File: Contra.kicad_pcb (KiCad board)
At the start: 2 copper layers, 251.5 x 76.2 mm, 152 parts, among them J1 Conn_01x03, J2 Conn_01x02, SW1 SW_PUSH, SW2 SW_SPDT, U1 ProMicro

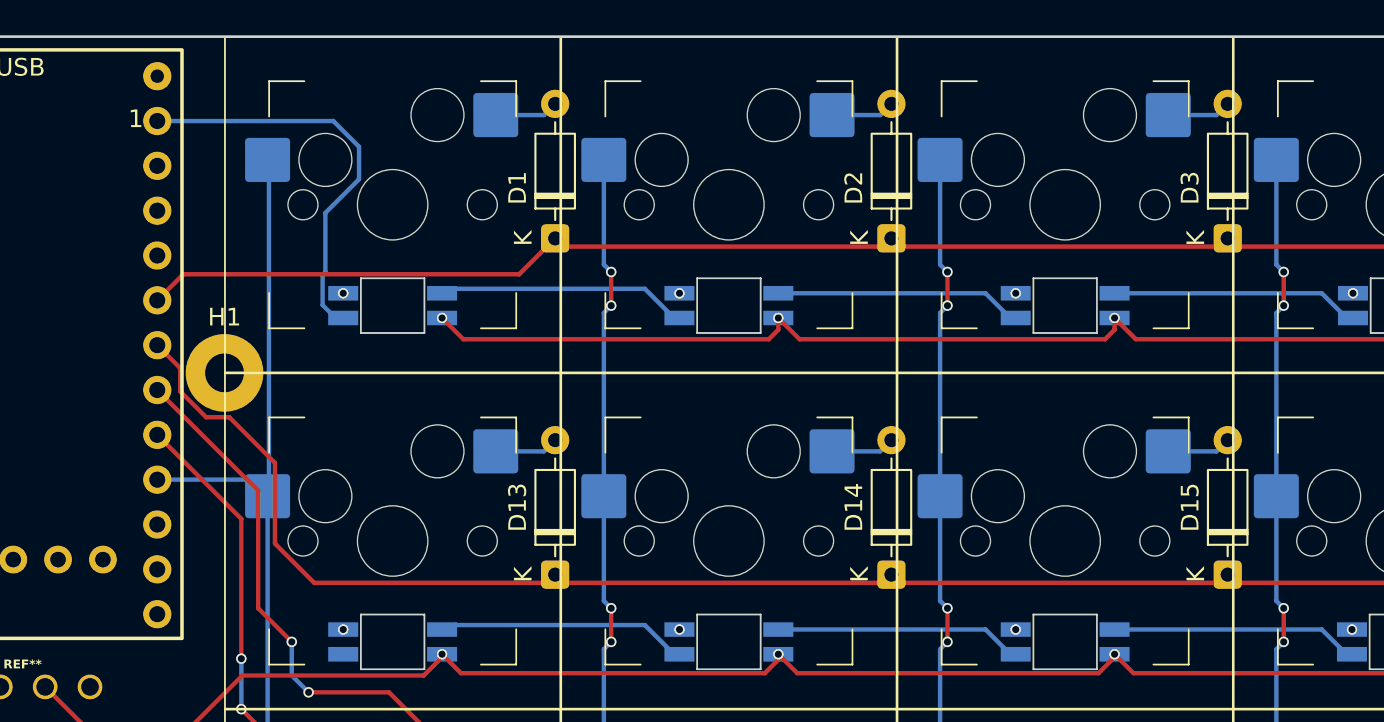
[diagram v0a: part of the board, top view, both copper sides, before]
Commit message: connect col1-3 to mcu
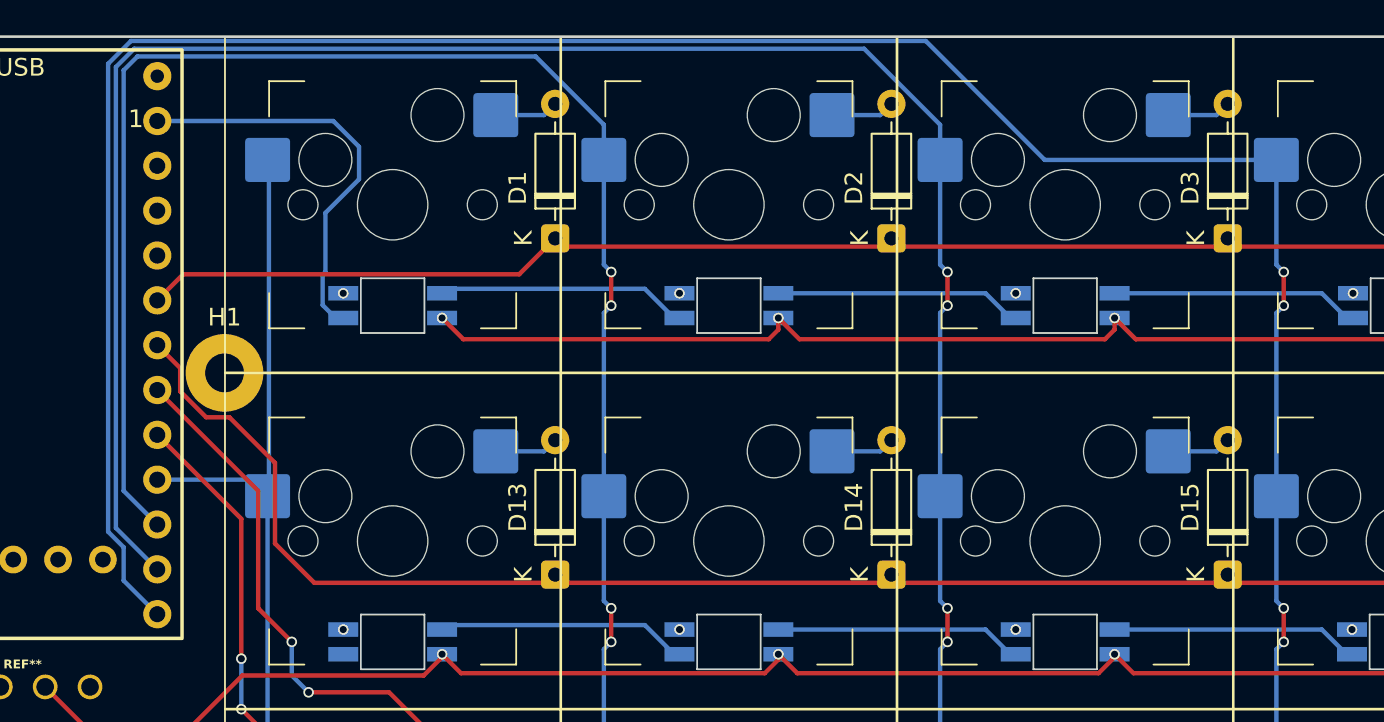
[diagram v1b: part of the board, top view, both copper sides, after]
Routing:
- net COL3: track 58.2 -> 160.0 mm
- net COL2: track 58.2 -> 138.5 mm
- net COL1: track 58.2 -> 115.8 mm
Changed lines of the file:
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@@
+	)
+	(segment
+		(start 39.831969 52.560531)
+		(end 39.0525 53.34)
+		(width 0.25)
+		(layer "B.Cu")
+		(net "COL1")
 	)
 	(segment
@@
 	)
 	(segment
+		(start 39.0525 77.170521)
+		(end 40.95751 79.075531)
+		(width 0.25)
+		(layer "B.Cu")
+		(net "COL1")
+	)
+	(segment
 		(start 66.2575 96.52)
 		(end 66.2575 86.1425)
@@
 	)
 	(segment
+		(start 66.2575 56.425651)
+		(end 62.39238 52.560531)
+		(width 0.25)
+		(layer "B.Cu")
+		(net "COL1")
+	)
+	(segment
+		(start 66.2575 58.42)
+		(end 66.2575 56.425651)
+		(width 0.25)
+		(layer "B.Cu")
+		(net "COL1")
+	)
+	(segment
 		(start 66.2575 115.57)
 		(end 66.2575 105.1925)
@@
 	)
 	(segment
+		(start 62.39238 52.560531)
+		(end 39.831969 52.560531)
+		(width 0.25)
+		(layer "B.Cu")
+		(net "COL1")
+	)
+	(segment
 		(start 66.2575 77.47)
 		(end 66.2575 67.0925)
@@
 	)
 	(segment
+		(start 39.0525 53.34)
+		(end 39.0525 77.170521)
+		(width 0.25)
+		(layer "B.Cu")
+		(net "COL1")
+	)
+	(segment
 		(start 66.675 83.82)
 		(end 66.2575 83.4025)
@@
 	)
 	(segment
+		(start 38.6125 53.157746)
+		(end 38.6125 79.270521)
+		(width 0.25)
+		(layer "B.Cu")
+		(net "COL2")
+	)
+	(segment
 		(start 85.3075 77.47)
 		(end 85.3075 67.0925)
@@
 	)
 	(segment
+		(start 85.3075 58.42)
+		(end 85.3075 56.425651)
+		(width 0.25)
+		(layer "B.Cu")
+		(net "COL2")
+	)
+	(segment
+		(start 81.00238 52.120531)
+		(end 39.649715 52.120531)
+		(width 0.25)
+		(layer "B.Cu")
+		(net "COL2")
+	)
+	(segment
 		(start 85.3075 115.57)
 		(end 85.3075 105.1925)
@@
 	)
 	(segment
+		(start 85.3075 56.425651)
+		(end 81.00238 52.120531)
+		(width 0.25)
+		(layer "B.Cu")
+		(net "COL2")
+	)
+	(segment
+		(start 39.649715 52.120531)
+		(end 38.6125 53.157746)
+		(width 0.25)
+		(layer "B.Cu")
+		(net "COL2")
+	)
+	(segment
 		(start 85.3075 64.3525)
 		(end 85.3075 58.42)
@@
 	)
 	(segment
+		(start 38.6125 79.270521)
+		(end 40.95751 81.615531)
+		(width 0.25)
+		(layer "B.Cu")
+		(net "COL2")
+	)
+	(segment
 		(start 104.775 83.82)
 		(end 104.775 85.725)
@@
 	)
 	(segment
+		(start 91.23415 58.42)
+		(end 84.494681 51.680531)
+		(width 0.25)
+		(layer "B.Cu")
+		(net "COL3")
+	)
+	(segment
+		(start 39.0525 82.250521)
+		(end 40.95751 84.155531)
+		(width 0.25)
+		(layer "B.Cu")
+		(net "COL3")
+	)
+	(segment
 		(start 104.3575 77.47)
 		(end 104.3575 83.4025)
@@
 	)
 	(segment
+		(start 39.0525 80.363672)
+		(end 39.0525 82.250521)
+		(width 0.25)
+		(layer "B.Cu")
+		(net "COL3")
+	)
+	(segment
 		(start 104.3575 58.42)
 		(end 104.3575 64.3525)
@@
 	)
 	(segment
+		(start 104.3575 58.42)
+		(end 91.23415 58.42)
+		(width 0.25)
+		(layer "B.Cu")
+		(net "COL3")
+	)
+	(segment
+		(start 38.1725 52.975492)
+		(end 38.1725 79.483672)
+		(width 0.25)
+		(layer "B.Cu")
+		(net "COL3")
+	)
+	(segment
 		(start 104.3575 67.0925)
 		(end 104.3575 77.47)
@@
 	)
 	(segment
+		(start 38.1725 79.483672)
+		(end 39.0525 80.363672)
+		(width 0.25)
+		(layer "B.Cu")
+		(net "COL3")
+	)
+	(segment
 		(start 104.775 66.675)
 		(end 104.3575 67.0925)
@@
 		(width 0.25)
 		(layer "B.Cu")
+		(net "COL3")
+	)
+	(segment
+		(start 84.494681 51.680531)
+		(end 39.467461 51.680531)
+		(width 0.25)
+		(layer "B.Cu")
+		(net "COL3")
+	)
+	(segment
+		(start 39.467461 51.680531)
+		(end 38.1725 52.975492)
+		(width 0.25)
+		(layer "B.Cu")

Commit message: tweak col3 track
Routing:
- net COL3: track 160.0 -> 161.6 mm
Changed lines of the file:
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@@
+	)
+	(segment
+		(start 39.467461 51.680531)
+		(end 38.1725 52.975492)
+		(width 0.25)
+		(layer "B.Cu")
+		(net "COL3")
+	)
+	(segment
+		(start 38.1725 79.483672)
+		(end 39.0525 80.363672)
+		(width 0.25)
+		(layer "B.Cu")
+		(net "COL3")
 	)
 	(segment
@@
 	)
 	(segment
-		(start 91.23415 58.42)
-		(end 84.494681 51.680531)
+		(start 100.258031 51.680531)
+		(end 39.467461 51.680531)
 		(width 0.25)
 		(layer "B.Cu")
@@
 	)
 	(segment
-		(start 39.0525 82.250521)
-		(end 40.95751 84.155531)
+		(start 104.3575 55.78)
+		(end 100.258031 51.680531)
 		(width 0.25)
 		(layer "B.Cu")
@@
 	)
 	(segment
-		(start 39.0525 80.363672)
-		(end 39.0525 82.250521)
-		(width 0.25)
-		(layer "B.Cu")
-		(net "COL3")
-	)
-	(segment
 		(start 104.3575 58.42)
 		(end 104.3575 64.3525)
@@
 	)
 	(segment
-		(start 104.3575 58.42)
-		(end 91.23415 58.42)
-		(width 0.25)
-		(layer "B.Cu")
-		(net "COL3")
-	)
-	(segment
-		(start 38.1725 52.975492)
-		(end 38.1725 79.483672)
+		(start 39.0525 82.250521)
+		(end 40.95751 84.155531)
 		(width 0.25)
 		(layer "B.Cu")
@@
 		(start 104.3575 67.0925)
 		(end 104.3575 77.47)
-		(width 0.25)
-		(layer "B.Cu")
-		(net "COL3")
-	)
-	(segment
-		(start 38.1725 79.483672)
-		(end 39.0525 80.363672)
 		(width 0.25)
 		(layer "B.Cu")
@@
 	)
 	(segment
-		(start 104.775 105.7275)
-		(end 104.3575 106.145)
+		(start 104.3575 58.42)
+		(end 104.3575 55.78)
 		(width 0.25)
 		(layer "B.Cu")
@@
 	)
 	(segment
-		(start 84.494681 51.680531)
-		(end 39.467461 51.680531)
+		(start 38.1725 52.975492)
+		(end 38.1725 79.483672)
 		(width 0.25)
 		(layer "B.Cu")
@@
 	)
 	(segment
-		(start 39.467461 51.680531)
-		(end 38.1725 52.975492)
+		(start 39.0525 80.363672)
+		(end 39.0525 82.250521)
 		(width 0.25)
 		(layer "B.Cu")
+		(net "COL3")
+	)
+	(segment
+		(start 104.775 105.7275)
+		(end 104.3575 106.145)
+		(width 0.25)
+		(layer "B.Cu")

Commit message: connect OLED to mcu
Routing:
- net Accessory1: track 0.00 -> 34.0 mm, vias 0 -> 1
- net Net-(OL1-SDA): track 0.00 -> 9.62 mm
- net Net-(OL1-SCL): track 0.00 -> 9.62 mm
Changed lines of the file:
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@@
 		(net "COL11")
+	)
+	(segment
+		(start 39.84251 59.870531)
+		(end 39.84251 89.37251)
+		(width 0.25)
+		(layer "F.Cu")
+		(net "Accessory1")
+	)
+	(segment
+		(start 40.95751 58.755531)
+		(end 39.84251 59.870531)
+		(width 0.25)
+		(layer "F.Cu")
+		(net "Accessory1")
+	)
+	(segment
+		(start 39.84251 89.37251)
+		(end 40.005 89.535)
+		(width 0.25)
+		(layer "F.Cu")
+		(net "Accessory1")
+	)
+	(via
+		(at 40.005 89.535)
+		(size 0.6)
+		(drill 0.4)
+		(layers "F.Cu" "B.Cu")
+		(net "Accessory1")
+	)
+	(segment
+		(start 39.0525 90.4875)
+		(end 39.0525 91.8175)
+		(width 0.25)
+		(layer "B.Cu")
+		(net "Accessory1")
+	)
+	(segment
+		(start 40.005 89.535)
+		(end 39.0525 90.4875)
+		(width 0.25)
+		(layer "B.Cu")
+		(net "Accessory1")
 	)
 	(via
@@
 		(net "Net-(LED46-DOUT)")
 	)
+	(segment
+		(start 37.87751 81.060731)
+		(end 37.87751 82.46499)
+		(width 0.25)
+		(layer "F.Cu")
+		(net "Net-(OL1-SCL)")
+	)
+	(segment
+		(start 37.87751 82.46499)
+		(end 32.0675 88.275)
+		(width 0.25)
+		(layer "F.Cu")
+		(net "Net-(OL1-SCL)")
+	)
+	(segment
+		(start 35.33751 81.060731)
+		(end 35.33751 82.46499)
+		(width 0.25)
+		(layer "F.Cu")
+		(net "Net-(OL1-SDA)")
+	)
+	(segment
+		(start 35.33751 82.46499)
+		(end 29.5275 88.275)
+		(width 0.25)
+		(layer "F.Cu")
+		(net "Net-(OL1-SDA)")
+	)
 	(zone

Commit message: connect col11 to mcu
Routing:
- net COL11: track 56.4 -> 350.2 mm
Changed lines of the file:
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@@
+	)
+	(segment
+		(start 24.6025 119.522254)
+		(end 24.6025 67.490521)
+		(width 0.25)
+		(layer "B.Cu")
+		(net "COL11")
 	)
 	(segment
 		(start 257.175 88.5825)
 		(end 256.7575 89)
+		(width 0.25)
+		(layer "B.Cu")
+		(net "COL11")
+	)
+	(segment
+		(start 42.441112 127.2825)
+		(end 32.362746 127.2825)
 		(width 0.25)
 		(layer "B.Cu")
@@
 	)
 	(segment
+		(start 24.6025 67.490521)
+		(end 25.7175 66.375521)
+		(width 0.25)
+		(layer "B.Cu")
+		(net "COL11")
+	)
+	(segment
+		(start 250.345 121.13)
+		(end 48.593612 121.13)
+		(width 0.25)
+		(layer "B.Cu")
+		(net "COL11")
+	)
+	(segment
 		(start 256.7575 77.47)
 		(end 256.7575 83.4025)
@@
 		(start 256.7575 64.3525)
 		(end 257.175 64.77)
+		(width 0.25)
+		(layer "B.Cu")
+		(net "COL11")
+	)
+	(segment
+		(start 255.905 115.57)
+		(end 250.345 121.13)
+		(width 0.25)
+		(layer "B.Cu")
+		(net "COL11")
+	)
+	(segment
+		(start 32.362746 127.2825)
+		(end 24.6025 119.522254)
 		(width 0.25)
 		(layer "B.Cu")
@@
 	)
 	(segment
+		(start 48.593612 121.13)
+		(end 42.441112 127.2825)
+		(width 0.25)
+		(layer "B.Cu")
+		(net "COL11")
+	)
+	(segment
 		(start 256.7575 58.42)
 		(end 256.7575 64.3525)
 		(width 0.25)
 		(layer "B.Cu")
+		(net "COL11")
+	)
+	(segment
+		(start 256.7575 115.57)
+		(end 255.905 115.57)
+		(width 0.25)
+		(layer "B.Cu")

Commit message: connect all cols to mcu
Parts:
- moved H1 8.57 mm to (44.8, 61.9)
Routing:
- net COL10: track 58.2 -> 274.5 mm, vias 6 -> 7
- net COL9: track 58.2 -> 254.8 mm, vias 6 -> 7
- net COL8: track 58.2 -> 236.0 mm, vias 6 -> 7
- net COL7: track 58.2 -> 217.3 mm, vias 6 -> 7
- net COL6: track 38.2 -> 179.7 mm, vias 4 -> 5
- net COL5: track 63.6 -> 187.6 mm, vias 6 -> 7
- net COL4: track 58.2 -> 164.9 mm, vias 6 -> 8
- net Accessory1: track 34.0 -> 0.00 mm, vias 1 -> 0
- net COL0: track 62.2 -> 72.8 mm
- net ROW1: track 230.4 -> 227.0 mm, vias 0 -> 1
- net ROW3: track 263.7 -> 264.7 mm, vias 2 -> 3
- net COL11: track 350.2 -> 349.4 mm
- net COL1: track 115.8 -> 116.6 mm
- net COL2: track 138.5 -> 137.9 mm
- net ROW2: track 240.9 -> 241.4 mm, vias 2 -> 3

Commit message: massage various tracks and finalize placements
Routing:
- net Net-(LED12-DOUT): track 0.00 -> 239.7 mm, vias 0 -> 2
- net Net-(LED24-DOUT): track 0.00 -> 237.2 mm, vias 0 -> 2
- net Accessory1: track 0.00 -> 48.2 mm, vias 0 -> 2
- net VBAT: track 1113.6 -> 1130.7 mm
- net COL0: track 72.8 -> 86.5 mm
- net ROW0: track 223.3 -> 226.3 mm
- net ROW2: track 241.4 -> 242.8 mm, vias 3 -> 1
- net ROW3: track 264.7 -> 263.7 mm, vias 3 -> 1

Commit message: Run DRC, fix errors
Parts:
- moved H1 0.09 mm to (44.8, 62.0)
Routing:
- net COL0: track 86.5 -> 79.9 mm
- net Accessory1: track 48.2 -> 49.1 mm
- net COL5: track 187.6 -> 188.1 mm
